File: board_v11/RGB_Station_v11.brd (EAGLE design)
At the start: 86.4 x 17.8 mm, 44 parts, among them IC1 MCP1702T-3302E/MB, J1 M20, J2 M20, J3 USB_MICRO, U1 PIC32MX270F256D_44VTLA_44, U2 74LVC2T45, U3 MCP121T-315E/TT, U4 DSC6111CI1A-008.0000, U6 RN4871

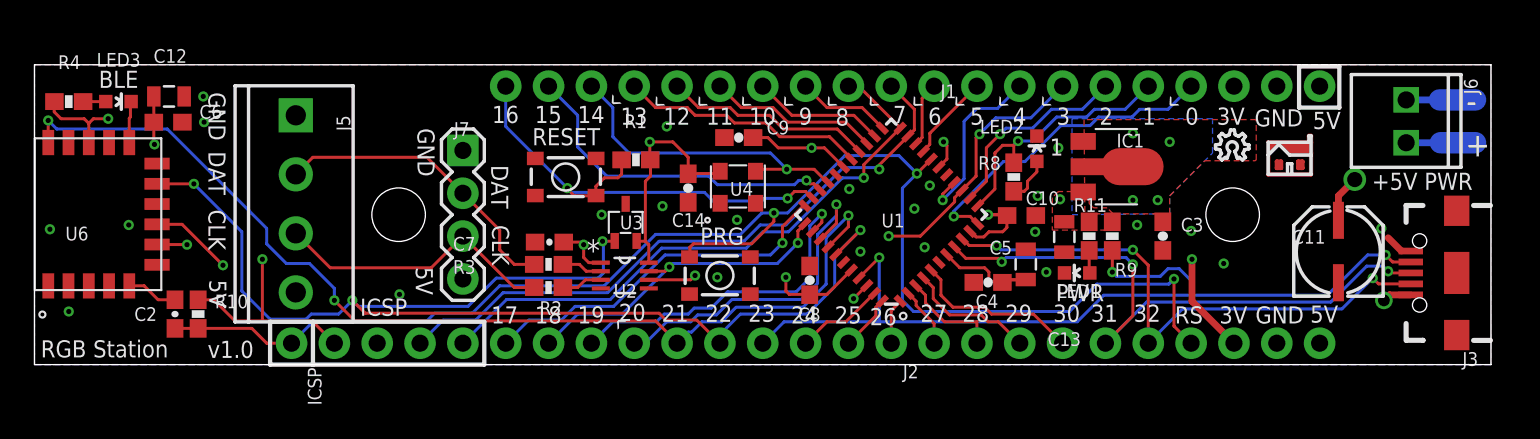
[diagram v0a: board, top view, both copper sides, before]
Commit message: Starting v1.1 of the board - changes listed in notes.txt
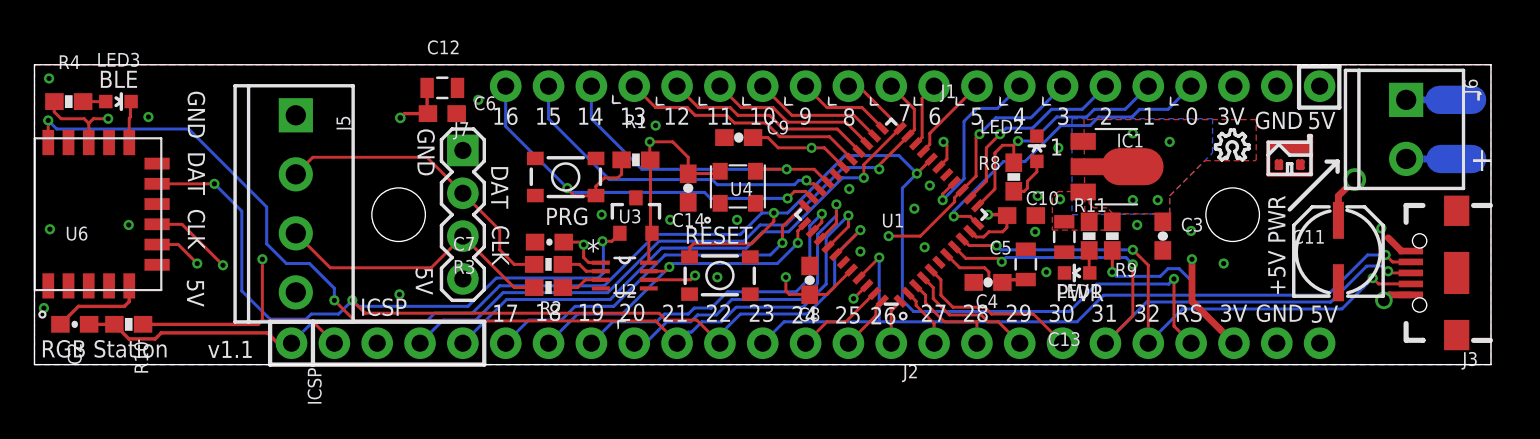
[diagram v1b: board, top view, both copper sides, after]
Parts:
- J6: device SparkFun-Connectors:1X02_2.54_SCREWTERM -> SparkFun-Connectors:SCREWTERMINAL-3.5MM-2
- U3: device MCP1x2_ResetController:SC70 -> MCP1x2_ResetController:SOT23-3
- moved C6 16.3 mm to (24.2, 14.9)
- moved C12 16.2 mm to (24.2, 16.4)
- moved C2 5.97 mm to (2.39, 2.39), turned to 0 degrees
- moved R10 4.16 mm to (5.59, 2.39), turned to 180 degrees
- moved U3 0.71 mm to (35.7, 8.79), turned to 0 degrees
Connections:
- net 3.3V: now also U3.2; no longer U3.P2
- net 5V: now also J6.2; no longer J6.P1
- net GND: now also J6.1, U3.3; no longer J6.P2, U3.P3
- net RST_N: now also U3.1; no longer U3.P1
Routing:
- net !MCLR!: track 86.6 -> 92.1 mm
- net 3.3V: track 164.5 -> 167.5 mm
- net N$8: track 3.06 -> 5.58 mm
- net RST_N: track 73.3 -> 74.5 mm
- net BT_RX: track 49.4 -> 50.3 mm
- net BT_MODE: track 62.3 -> 63.1 mm
- net 5V: track 111.6 -> 111.0 mm
- net GND: track 5.78 -> 5.57 mm, vias 24 -> 25
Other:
- board text added: "v1.1"
- board text removed: "v1.0"

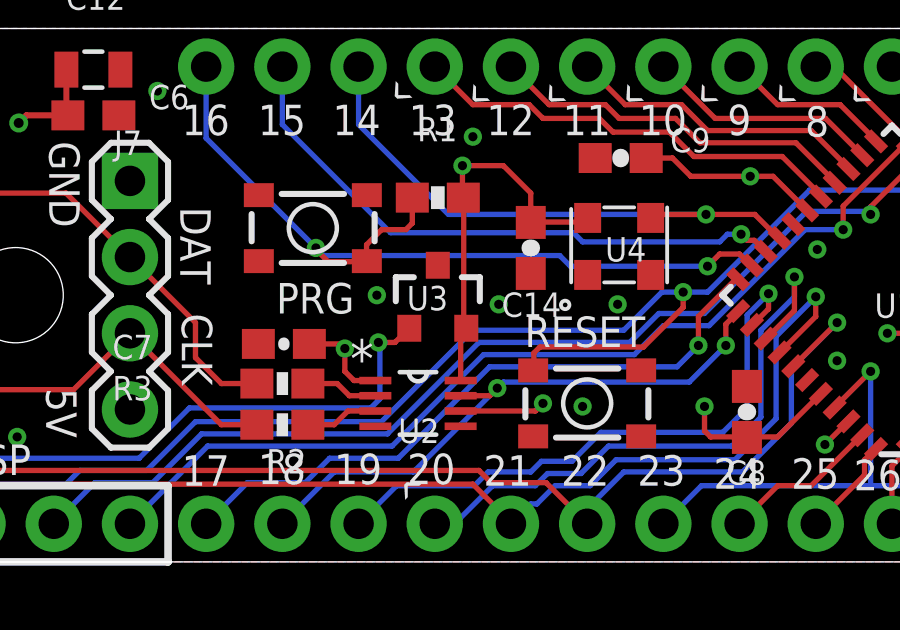
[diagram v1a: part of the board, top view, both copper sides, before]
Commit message: Updated switches with proper footprint.
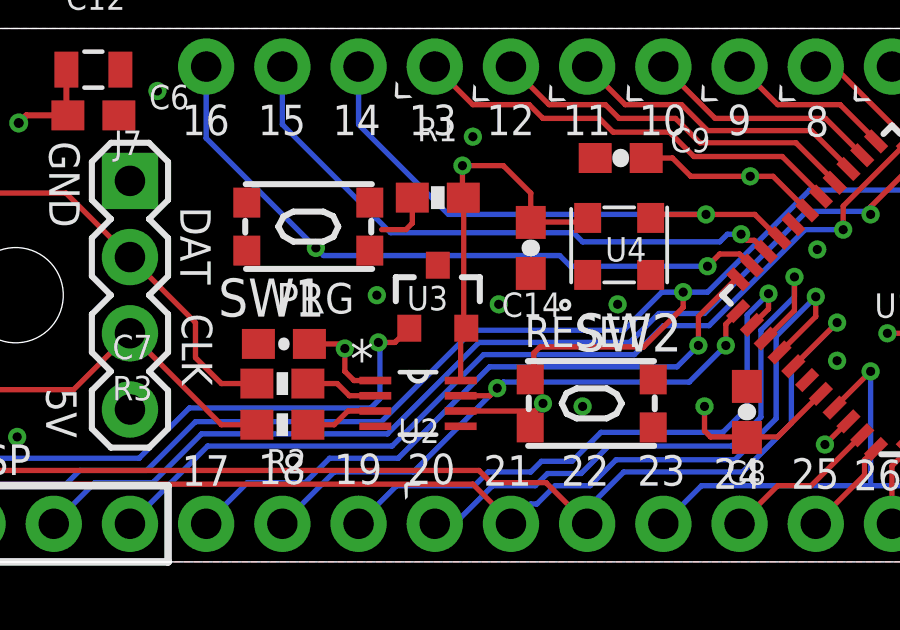
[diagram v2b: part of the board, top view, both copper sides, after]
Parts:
- removed S1, S2: SWITCH-MOMENTARY-SPSTSMD-3, SparkFun-Retired:TACTILE_SWITCH_SMD-3
- added SW1, SW2: KMR2_SWITCH, kmr2_switch:KMR2_SWITCH
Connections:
- net !MCLR!: now also SW2.P3, SW2.P4; no longer S2.4
- net GND: now also SW1.P1, SW1.P2, SW2.P1, SW2.P2; no longer S1.1, S2.1
- net RA8: now also SW1.P3, SW1.P4; no longer S1.4
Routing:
- net RA8: track 27.8 -> 24.6 mm
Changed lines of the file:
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@@
 <?xml version="1.0" encoding="utf-8"?>
 <!DOCTYPE eagle SYSTEM "eagle.dtd">
-<eagle version="7.7.0">
+<eagle version="6.6.0">
 <drawing>
 <settings>
@@
 <layer number="14" name="Route14" color="1" fill="6" visible="no" active="no"/>
 <layer number="15" name="Route15" color="4" fill="6" visible="no" active="yes"/>
-<layer number="16" name="Bottom" color="1" fill="1" visible="yes" active="yes"/>
+<layer number="16" name="Bottom" color="1" fill="1" visible="no" active="yes"/>
 <layer number="17" name="Pads" color="2" fill="1" visible="yes" active="yes"/>
 <layer number="18" name="Vias" color="2" fill="1" visible="yes" active="yes"/>
@@
 <pass name="Default">
 <param name="RoutingGrid" value="50mil"/>
-<param name="AutoGrid" value="1"/>
-<param name="Efforts" value="0"/>
-<param name="TopRouterVariant" value="1"/>
 <param name="tpViaShape" value="round"/>
 <param name="PrefDir.1" value="|"/>
@@
 <attribute name="PROD_ID" value="CONN-08399" x="81.3308" y="15.6972" size="1.778" layer="27" rot="R270" display="off"/>
 </element>
-<element name="S1" library="SparkFun-Retired" package="TACTILE_SWITCH_SMD-3" value="SWITCH-MOMENTARY-SPSTSMD-3" x="31.496" y="11.1252" smashed="yes"/>
-<element name="S2" library="SparkFun-Retired" package="TACTILE_SWITCH_SMD-3" value="SWITCH-MOMENTARY-SPSTSMD-3" x="40.64" y="5.2832" smashed="yes" rot="R180"/>
 <element name="U3" library="MCP1x2_ResetController" package="SOT23-3" value="MCP121T-315E/TT" x="35.6616" y="8.7884" smashed="yes">
 <attribute name="NAME" x="36.0012" y="9.1976" size="0.8128" layer="25" font="vector" ratio="10" rot="R180"/>
@@
 <attribute name="VALUE" x="40.044" y="12.1304" size="0.8128" layer="27" font="vector" ratio="10" rot="R90"/>
 </element>
+<element name="SW1" library="kmr2_switch" package="KMR2_SWITCH" value="KMR2_SWITCH" x="31.3436" y="11.176"/>
+<element name="SW2" library="kmr2_switch" package="KMR2_SWITCH" value="KMR2_SWITCH" x="40.7924" y="5.2832" rot="R180"/>
 </elements>
 <signals>
@@
 <contactref element="U6" pad="13"/>
 <contactref element="U3" pad="3"/>
-<contactref element="S1" pad="1"/>
-<contactref element="S2" pad="1"/>
 <contactref element="J3" pad="SHIELD1"/>
 <contactref element="J3" pad="SHIELD2"/>
@@
 <wire x1="81.3308" y1="15.6972" x2="83.312" y2="15.6972" width="0.4064" layer="16"/>
 <wire x1="83.312" y1="15.6972" x2="85.2424" y2="15.6972" width="1.6764" layer="16"/>
+<contactref element="SW1" pad="P1"/>
+<contactref element="SW2" pad="P1"/>
+<contactref element="SW1" pad="P2"/>
+<contactref element="SW2" pad="P2"/>
+<wire x1="42.8424" y1="6.0832" x2="42.8424" y2="4.4832" width="0" layer="19" extent="1-1"/>
 </signal>
 <signal name="3.3V">
@@
 <wire x1="52.1208" y1="3.1496" x2="51.4604" y2="3.81" width="0.1778" layer="16"/>
 <wire x1="51.4604" y1="3.81" x2="51.4604" y2="10.4648" width="0.1778" layer="16"/>
-<contactref element="S2" pad="4"/>
 <contactref element="C2" pad="2"/>
 <wire x1="52.324" y1="11.3284" x2="51.4604" y2="10.4648" width="0.1778" layer="16"/>
@@
 <wire x1="39.0652" y1="7.1628" x2="38.862" y2="6.9596" width="0.1778" layer="1"/>
 <wire x1="38.862" y1="6.9596" x2="38.862" y2="6.4052" width="0.1778" layer="1"/>
-<wire x1="38.862" y1="6.4052" x2="38.84" y2="6.3832" width="0.1778" layer="1"/>
 <wire x1="44.6532" y1="8.9916" x2="48.0568" y2="12.3952" width="0.1778" layer="16"/>
 <wire x1="3.2376" y1="2.3876" x2="4.738" y2="2.3876" width="0.2032" layer="1"/>
@@
 <wire x1="7.1628" y1="1.524" x2="5.6016" y2="1.524" width="0.2032" layer="1"/>
 <wire x1="5.6016" y1="1.524" x2="4.738" y2="2.3876" width="0.2032" layer="1"/>
+<contactref element="SW2" pad="P4"/>
+<contactref element="SW2" pad="P3"/>
+<wire x1="42.5196" y1="7.1628" x2="38.7424" y2="4.4832" width="0" layer="19" extent="1-1"/>
+<wire x1="38.7424" y1="6.0832" x2="38.7424" y2="4.4832" width="0" layer="19" extent="1-1"/>
 </signal>
 <signal name="RB13">
@@
 <wire x1="45.72" y1="10.2616" x2="45.0596" y2="10.2616" width="0.1778" layer="1"/>
 <wire x1="44.6532" y1="9.8552" x2="45.0596" y2="10.2616" width="0.1778" layer="1"/>
-<contactref element="S1" pad="4"/>
 <wire x1="31.8516" y1="10.2108" x2="31.5976" y2="10.4648" width="0.1778" layer="16"/>
 <via x="31.5976" y="10.4648" extent="1-16" drill="0.3048"/>
-<wire x1="31.5976" y1="10.4648" x2="31.5976" y2="10.414" width="0.1778" layer="1"/>
-<wire x1="31.5976" y1="10.414" x2="32.004" y2="10.0076" width="0.1778" layer="1"/>
-<wire x1="32.004" y1="10.0076" x2="33.2784" y2="10.0076" width="0.1778" layer="1"/>
-<wire x1="33.2784" y1="10.0076" x2="33.296" y2="10.0252" width="0.1778" layer="1"/>
+<wire x1="31.5976" y1="10.4648" x2="31.5976" y2="10.414" width="0" layer="19" extent="1-16"/>
+<wire x1="31.5976" y1="10.414" x2="32.004" y2="10.0076" width="0" layer="19" extent="1-16"/>
+<wire x1="32.004" y1="10.0076" x2="33.2784" y2="10.0076" width="0" layer="19" extent="1-16"/>
 <wire x1="34.8116" y1="12.1412" x2="34.8116" y2="11.2912" width="0.1778" layer="1"/>
 <wire x1="34.8116" y1="11.2912" x2="34.5948" y2="11.0744" width="0.1778" layer="1"/>
 <wire x1="34.5948" y1="11.0744" x2="33.7884625" y2="11.0744" width="0.1778" layer="1"/>
-<wire x1="33.7884625" y1="11.0744" x2="33.28714375" y2="10.57308125" width="0.1778" layer="1"/>
-<wire x1="33.28714375" y1="10.57308125" x2="33.28714375" y2="10.03405625" width="0.1778" layer="1"/>
-<wire x1="33.28714375" y1="10.03405625" x2="33.296" y2="10.0252" width="0.1778" layer="1"/>
+<wire x1="33.7884625" y1="11.0744" x2="33.28714375" y2="10.57308125" width="0" layer="19" extent="1-16"/>
+<wire x1="33.28714375" y1="10.57308125" x2="33.28714375" y2="10.03405625" width="0" layer="19" extent="1-16"/>
 <wire x1="27.94" y1="16.51" x2="27.94" y2="14.1224" width="0.1778" layer="16"/>
 <wire x1="27.94" y1="14.1224" x2="31.5976" y2="10.4648" width="0.1778" layer="16"/>
+<contactref element="SW1" pad="P4"/>
+<contactref element="SW1" pad="P3"/>
+<wire x1="33.7884625" y1="11.0744" x2="33.3936" y2="11.976" width="0" layer="19" extent="1-1"/>
+<wire x1="33.2784" y1="10.0076" x2="33.28714375" y2="10.03405625" width="0" layer="19" extent="1-1"/>
+<wire x1="33.3936" y1="10.376" x2="33.28714375" y2="10.57308125" width="0" layer="19" extent="1-1"/>
 </signal>
 <signal name="RC2">

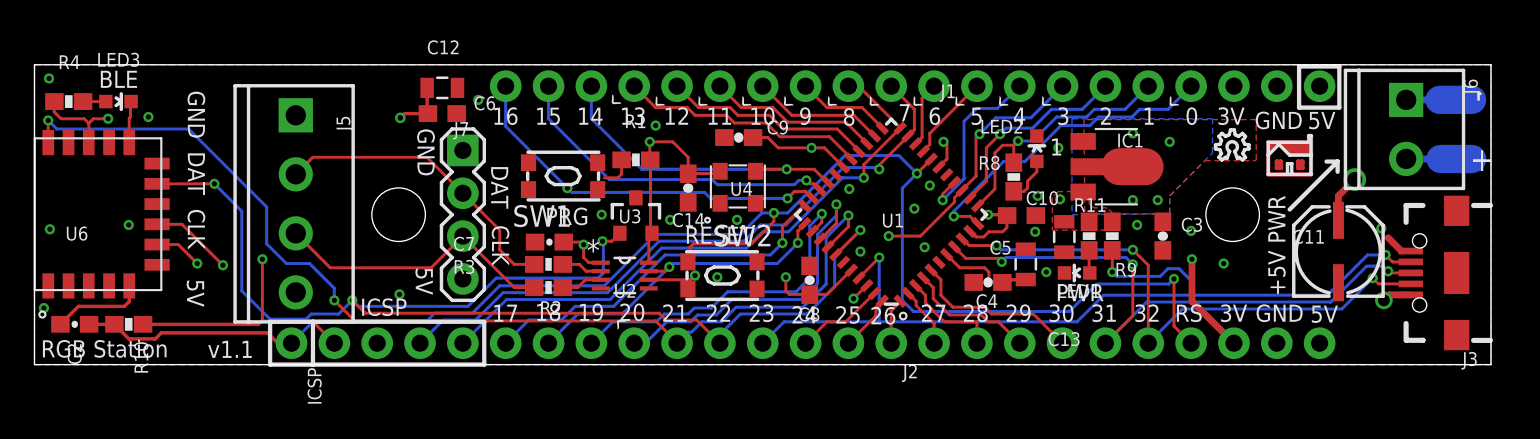
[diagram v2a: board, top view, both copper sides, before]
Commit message: Routed new switches, tweaked layout a bit - blue LED now on very end.
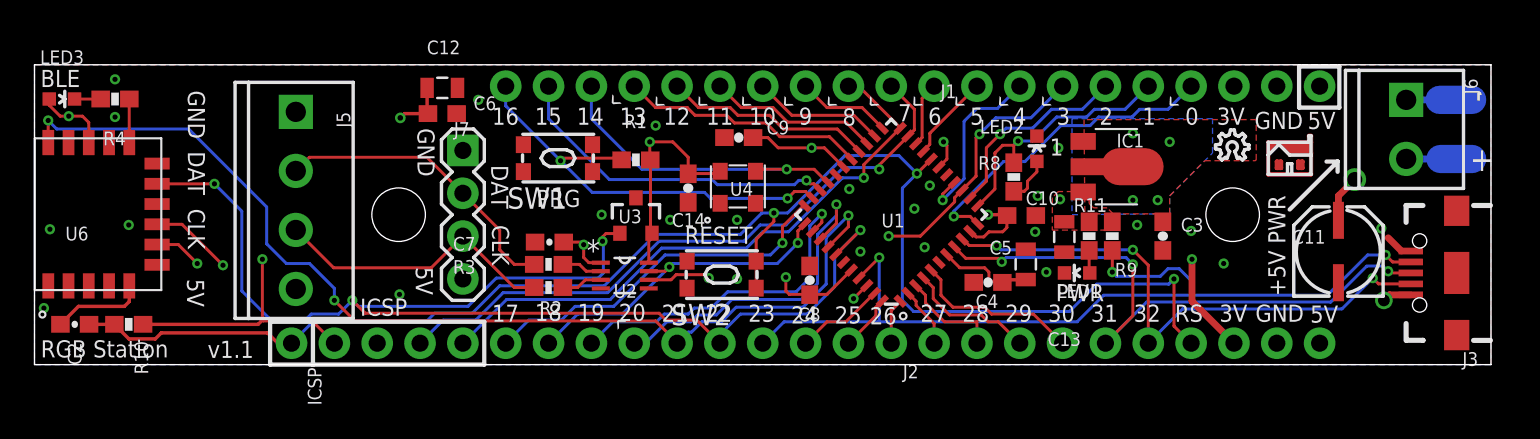
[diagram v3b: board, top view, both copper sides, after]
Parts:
- R11, R4, R8: value 1K -> 8.2K
- moved LED3 3.36 mm to (1.63, 15.7)
- moved R4 2.75 mm to (4.78, 15.7), turned to 0 degrees
- moved SW1 1.11 mm to (31.0, 12.2)
- moved J5 0.20 mm to (15.5, 15.0)
- moved SW2 0.07 mm to (40.7, 5.33), turned to 0 degrees
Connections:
- removed net N$10: LED3.A, R4.1
- removed net N$9: LED3.C, U6.12
- new net N$1: R4.2, U6.12
- new net N$5: LED3.C, R4.1
- net 3.3V: now also LED3.A; no longer R4.2
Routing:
- net RA8: track 24.6 -> 27.4 mm
- net N$1: track 0.00 -> 2.58 mm
- net N$9: track 2.47 -> 0.00 mm
- net !MCLR!: track 92.0 -> 90.3 mm
- net N$5: track 0.00 -> 1.55 mm
- net N$10: track 1.35 -> 0.00 mm
- net 3.3V: track 167.5 -> 168.6 mm

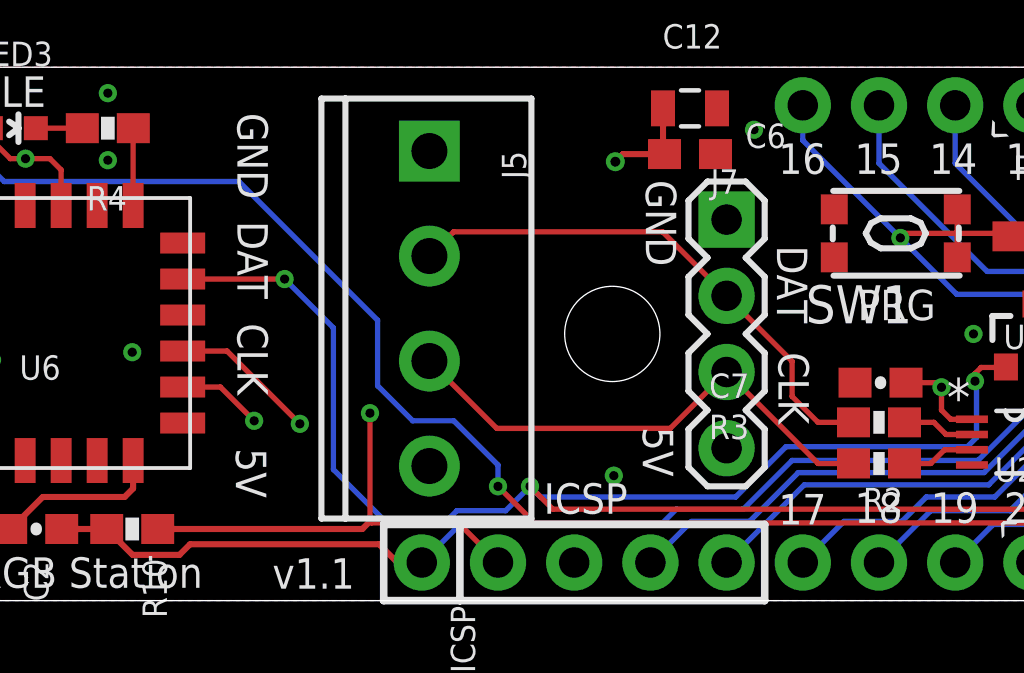
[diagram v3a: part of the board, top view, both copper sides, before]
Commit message: Added pin numbers to CLK and DAT output silk screen
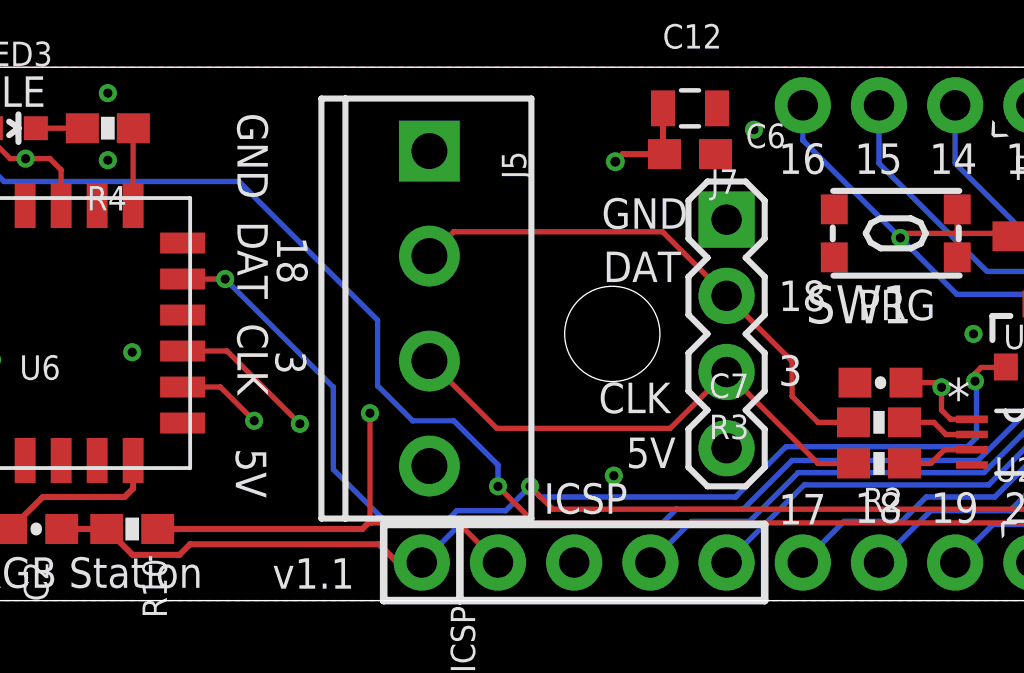
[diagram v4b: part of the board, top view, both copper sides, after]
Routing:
- net RST_N: track 74.6 -> 73.5 mm

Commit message: Version 1.1 complete and ready for fab.
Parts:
- R2, R3: value 333 -> 100
- moved U$3 4.02 mm to (64.7, 8.78)
- moved U$2 0.22 mm to (76.2, 7.83)
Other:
- board text added: "5V power"
- board text removed: "Only 5V power USB or terminals"
